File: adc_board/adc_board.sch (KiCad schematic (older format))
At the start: 47 parts, among them U4 HY3131, U8 ITX0505SA, U9 74HC595

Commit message: More work on ADC board schematics
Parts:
- removed R? (x3): R, symbol Device:R
- added C14, C7: 27nF, symbol Device:C
- added C19, C2, C25, C26, C3, C4, C6: C, symbol Device:C
- added F?: Fuse, symbol Device:Fuse
- added R10, R14, R3: 2.5M, symbol Device:R
- added R11: 20k, symbol Device:R
- added R17, R45, R62: 100, symbol Device:R
- added R2, R8, R9: 270k, symbol Device:R
- added R26: 56k, symbol Device:R
- added R28, R31: 90k, symbol Device:R
- added R30, R32: 10k, symbol Device:R
- added R34, R51, R52: 1k, symbol Device:R
- added R36: 1M, symbol Device:R
- added R76: 0, symbol Device:R
- R18: renamed from R?; value R -> 2.5M
- R19: renamed from R?; value R -> 1M
- R20: renamed from R?; value R -> 100k
- R21: renamed from R?; value R -> 10k
- R22, R24: renamed from R?; value R -> 1k
- R23: renamed from R?; value R -> 10M
- R?: value R -> 1
- Y?: value Crystal -> 4 MHz
- gave numbers to parts that had none: 2
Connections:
- net labels added: CNT, GND, VSSA
- wire segments 0 -> 142
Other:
- moved on the sheet: C02, C03, C04, C06, C07, D?, F?, K?, R19, R20, R21, R22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

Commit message: Map out U2 on ADC board
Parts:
- removed R?: 1, symbol Device:R
- added C?: CP, symbol Device:CP
- added R13, R15: 10k, symbol Device:R
- added R6: 100, symbol Device:R
- added R60: 750, symbol Device:R
- added R7: 1, symbol Device:R_Shunt
- added U2: SGM3157, Package_TO_SOT_SMD:SOT-363_SC-70-6, symbol Analog_Switch:FSA3157P6X
- R41: renamed from R?; value R -> 430
- R42: renamed from R?; value R -> 820
- U8: value ITX0505SA -> F0505S-1W
- gave numbers to parts that had none: 2
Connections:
- net labels added: PB1, U19_CTRL, VDD
- wire segments 142 -> 191
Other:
- note added: "VDD = 3.6 V"
- moved on the sheet: K?, R41, R42, U8, U9, U?

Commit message: Map out ADC board digital connections & DGND
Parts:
- removed U? (x5): ILD74, symbol Isolator:ILD74
- added C38, C42, C8, C?: C, symbol Device:C
- added D1, D2, D3, D4, D5: D, symbol Device:D
- added L1, L3, L4: Ferrite, symbol Device:L_Core_Ferrite
- added Q1, Q2, Q5: NPN, symbol Device:Q_NPN_BCE
- added R1, R46: 10, symbol Device:R
- added R16, R43, R44: 1k, symbol Device:R
- added R40, R?: 2k, symbol Device:R
- added R55: 330, symbol Device:R
- added R64, R65, R66, R75, R?: 470, symbol Device:R
- added U12: EL357, Package_DIP:DIP-4_W7.62mm, symbol Isolator:SFH617A-1
- added U15, U16: ELD207, Package_DIP:DIP-8_W7.62mm, symbol Isolator:LTV-827
- C13: renamed from C?; value CP -> 220uF
- gave numbers to parts that had none: 5
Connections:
- net labels added: +5V, GNDA, GNDD, GNDPWR, MCU_MISO, MCU_MOSI, MCU_NSS1, MCU_NSS2, MCU_SCK, MISO, MOSI, NSS1, NSS2, RL1_CTRL, RL2_CTRL, SCK, U1_CTRL, U2_CTRL, VDD_MCU
- wire segments 191 -> 316
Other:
- note added: "NOTE: GNDA = GNDD + 3.3V"
- note added: "Regulator voltage 3.6 V\nDiode drop 0.3 V"
- note added: "U3 is apparently overcurrent\nprotection for the low current side."
- note removed: "VDD = 3.6 V"
- moved on the sheet: C03, C05, C13, J?, R41, R42, U8, U?

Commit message: Map remaining connections on ADC board
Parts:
- removed D5: D, symbol Device:D
- removed F?: Polyfuse, symbol Device:Polyfuse
- added C10, C20, C21, C22, C30, C34, C41, C9: C, symbol Device:C
- added D5: Diode, symbol Device:D_x2_Serial_ACK
- added Q3, Q4: NPN, symbol Device:Q_NPN_BCE
- added R25: 100, symbol Device:R
- added R29, R35, R56: 2k, symbol Device:R
- added R5: PTC 1kohm, symbol Device:Thermistor_PTC
- added U17: MAX6071AAUT12, Package_TO_SOT_SMD:SOT-23-6, symbol Reference_Voltage:REF3230AMDBVREP
- U13: renamed from J?; value Conn_01x16 -> To MCU board
- gave numbers to parts that had none: 13
- renumbered C38 to C36
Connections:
- net +5V: now also R25.2
- net GNDA: now also C20.1, C21.2, D5.2 (common), Q4.3 (E)
- net GNDD: now also U9.13 (~OE), C20.2, C21.1, C22.2, C34.2, D5.1 (A), R29.2, R35.2, R56.2
- net MOSI: now also R29.1
- net NSS1: now also R56.1
- net SCK: now also R35.1
- net VDD: now also D5.3 (K)
- net at C14.1, R17.2: now also Q3.3 (E), R5.1
- net at R19.2, U4.39 (PA7): now also C41.1
- net at U4.4 (REFO): now also C9.2
- net at C3.2, R19.1, R20.1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: now also C41.2
- net VREF_1.25: now reaches U4.7 (PB6)
- net VREF_1.25: now also C10.2, U17.5 (OUT_S), U17.6 (OUT_F)
- net at RL1.8: now also R5.2
- net at Q1.2 (C): now also R46.2
- new net: C10.1, C30.2, C9.1, U17.1 (GNDF), U17.2 (GNDS)
- new net: C22.1, C30.1, C34.1, R25.1, U17.3 (ENABLE), U17.4 (VIN)
- new net: Q3.1 (B), Q3.2 (C), Q4.1 (B), Q4.2 (C)
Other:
- note added: "1.25 V reference"
- note added: "NOTE: GNDA is floating relative to GNDD,\nand usually settles at GNDA = VDD + 0.4V"
- note added: "VDD = 3.4 V"
- note removed: "NOTE: GNDA = GNDD + 3.3V"
- note removed: "Regulator voltage 3.6 V\nDiode drop 0.3 V"

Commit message: Clean up ADC board schematic
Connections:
- net GND is gone; now on net GNDA: C03.1 (Pin_1)
- net GNDA: now also R32.1; no longer R32.2
- net VDD: now also D2.1 (K), RL2.10
- net VSSA: now also C10.1, C30.2, C6.2, C8.1, C9.1, R55.2, U17.1 (GNDF), U17.2 (GNDS), U4.3 (AGND); no longer C6.1
- net PB2: now reaches C26.1, R52.1, U4.11 (PB2)
- net at U4.13 (ACM): now also C6.1; no longer C6.2
- net PB0: now reaches R11.2, U4.16 (PB0)
- net at U4.17 (PB8): now also R26.2
- net OP1N: now reaches U4.18 (OP1N)
- net OP1N: now also R28.2, R30.2; no longer R26.2
- net OP1O: now reaches C4.2, R28.1, U4.19 (OP1O)
- net OP2N: now reaches R31.2
- net OP2N: now also R32.2, U4.20 (OP2N); no longer U4.21 (OP2O)
- net PB5: now reaches C26.2, R51.1, U4.8 (PB5)
- net PB4: now reaches C4.1, R36.2, U4.9 (PB4)
- net at RL1.4: now also RL1.7
- net at Q2.2 (C): now also R1.2
- new net OP2O: R31.1, U4.21 (OP2O)
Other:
- note added: "4-wire resistance sense"
- note added: "Current measurement"
- note added: "Power supply isolation"
- note added: "Relay control"
- note added: "SPI isolation"
- note added: "U3 is overcurrent protection\nfor the low current shunts."
- note added: "Voltage measurement"
- note removed: "U3 is apparently overcurrent\nprotection for the low current side."
- moved on the sheet: C02, C03, C04, C05, C06, C07, C10, C13, C14, C19, C2, C20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

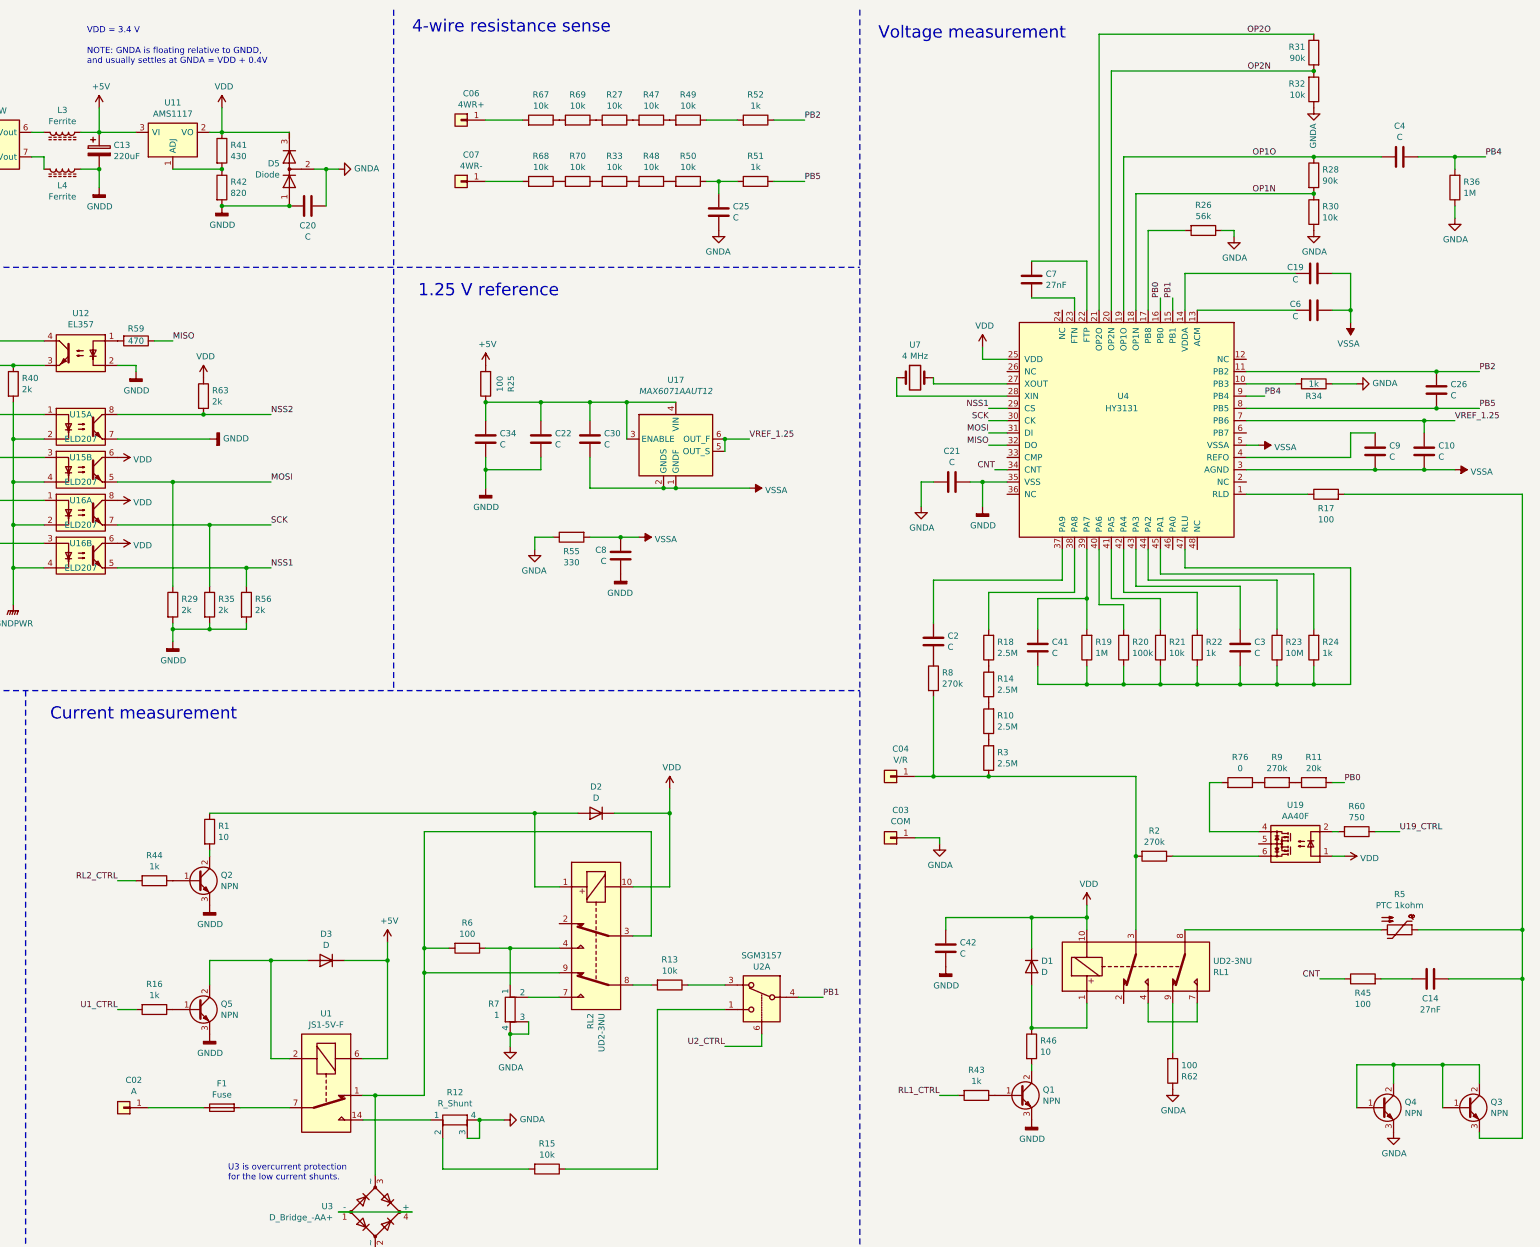
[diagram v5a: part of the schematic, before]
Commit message: ADC board schematic: fix GNDA/VSSA mixup
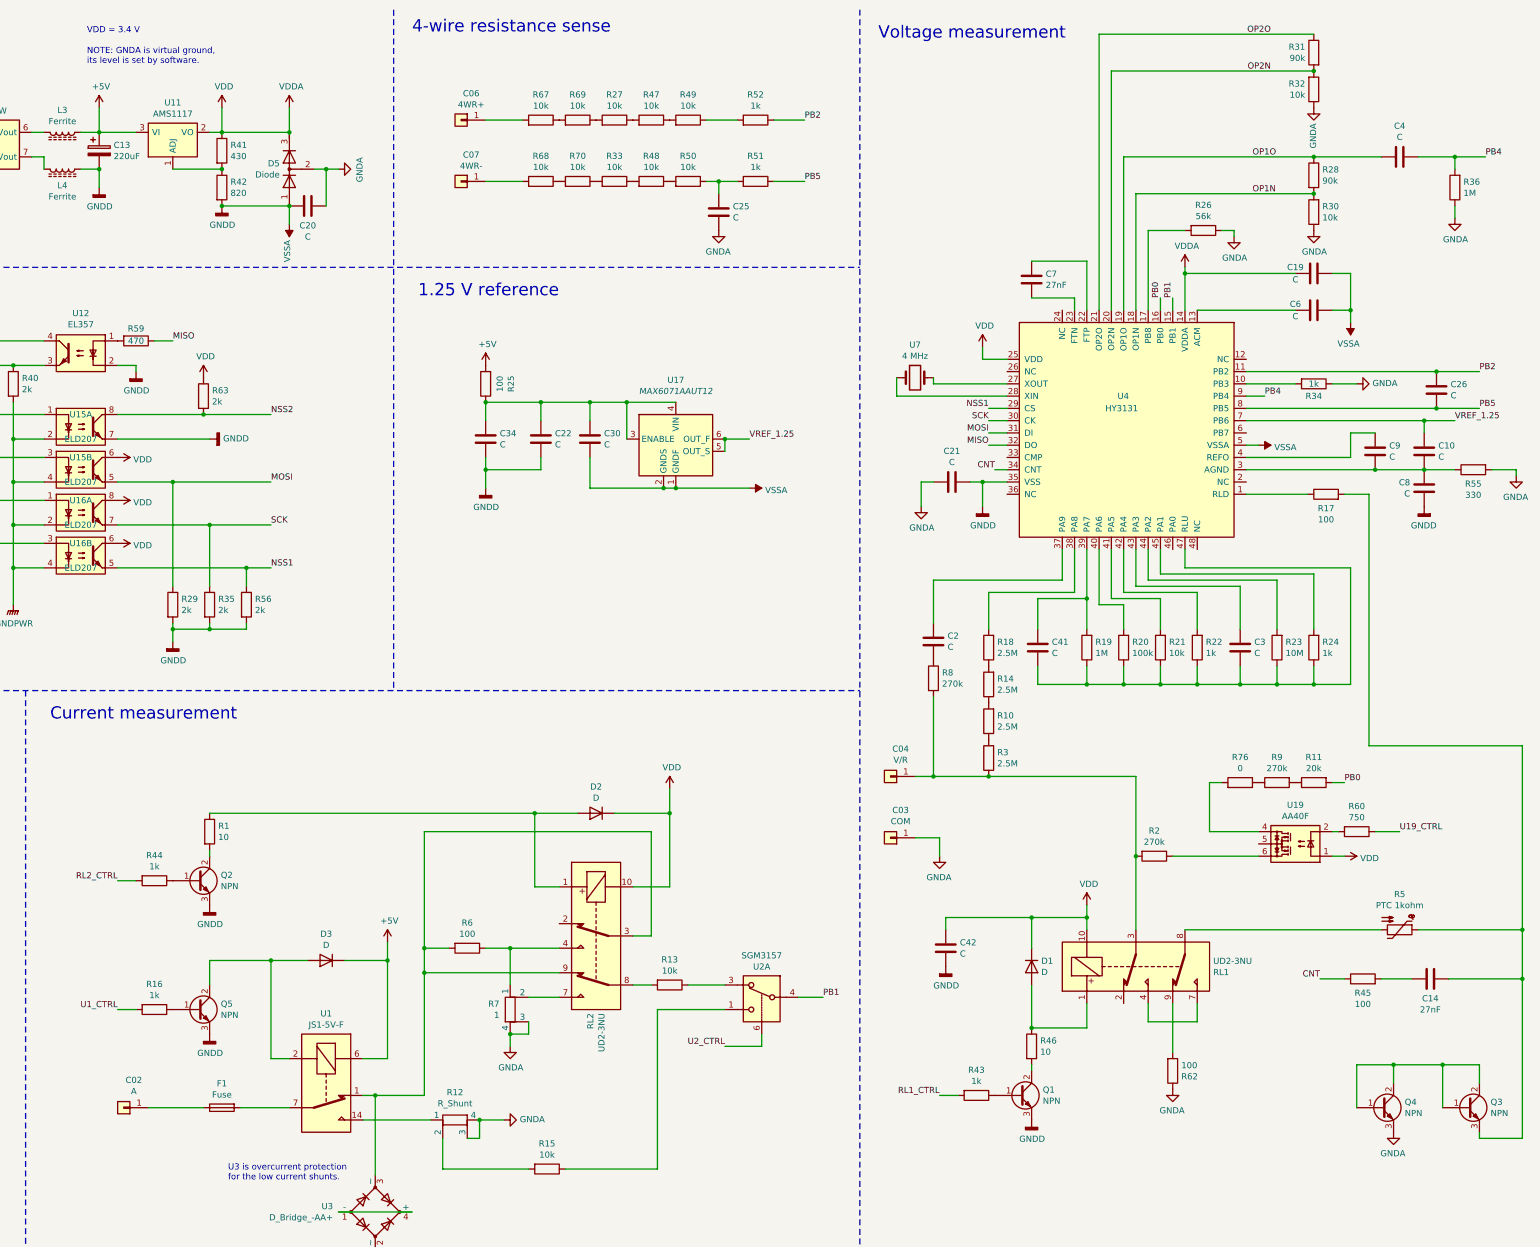
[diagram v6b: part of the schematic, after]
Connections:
- net GNDA: now also R55.2; no longer R55.1
- net GNDD: now also C19.1, C30.2, C6.2, U17.1 (GNDF), U17.2 (GNDS), U4.5 (VSSA)
- net VDD: now also C19.2, U4.14 (VDDA)
- removed net VSSA: C10.1, C19.1, C30.2, C6.2, C8.1, C9.1, R55.2, U17.1 (GNDF), U17.2 (GNDS), U4.3 (AGND), U4.5 (VSSA)
- new net: C10.1, C8.1, C9.1, R55.1, U4.3 (AGND)
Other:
- note added: "NOTE: GNDA is virtual ground,\nits level is set by software."
- note removed: "NOTE: GNDA is floating relative to GNDD,\nand usually settles at GNDA = VDD + 0.4V"
- moved on the sheet: C8, R55
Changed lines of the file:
@@
 Sheet 1 1
 Title "XDM2041 ADC board"
-Date "2021-08-12"
+Date "2022-01-18"
 Rev ""
 Comp ""
@@
 	11900 6000 12200 6000
 Wire Wire Line
-	10400 7300 10400 7250
-Wire Wire Line
 	10400 7250 10200 7250
 $Comp
@@
 Connection ~ 3550 1500
 Text Notes 3450 950  0    50   ~ 0
-NOTE: GNDA is floating relative to GNDD,\nand usually settles at GNDA = VDD + 0.4V
-$Comp
-L power:GNDA #PWR0108
-U 1 1 6140A326
-P 5500 1800
-F 0 "#PWR0108" H 5500 1550 50  0001 C CNN
-F 1 "GNDA" V 5505 1672 50  0000 R CNN
-F 2 "" H 5500 1800 50  0001 C CNN
-F 3 "" H 5500 1800 50  0001 C CNN
-	1    5500 1800
-	0    -1   -1   0
-$EndComp
+NOTE: GNDA is virtual ground,\nits level is set by software.
 $Comp
 L power:GNDA #PWR0109
@@
 $EndComp
 $Comp
-L power:GNDA #PWR0121
-U 1 1 61447E7F
-P 12300 9300
-F 0 "#PWR0121" H 12300 9050 50  0001 C CNN
-F 1 "GNDA" H 12305 9127 50  0000 C CNN
-F 2 "" H 12300 9300 50  0001 C CNN
-F 3 "" H 12300 9300 50  0001 C CNN
-	1    12300 9300
-	1    0    0    -1
-$EndComp
-$Comp
 L power:GNDA #PWR0122
 U 1 1 6144821F
@@
 $EndComp
 $Comp
-L power:GNDA #PWR0125
-U 1 1 61448B22
-P 14600 2200
-F 0 "#PWR0125" H 14600 1950 50  0001 C CNN
-F 1 "GNDA" H 14605 2027 50  0000 C CNN
-F 2 "" H 14600 2200 50  0001 C CNN
-F 3 "" H 14600 2200 50  0001 C CNN
-	1    14600 2200
-	1    0    0    -1
-$EndComp
-$Comp
 L power:GNDA #PWR0126
 U 1 1 61449089
@@
 Wire Wire Line
 	5500 1800 5400 1800
-Wire Wire Line
-	5100 2100 4550 2100
 Connection ~ 4550 2100
 Wire Wire Line
@@
 F 3 "~" H 14000 9450 50  0001 C CNN
 	1    14000 9450
-	1    0    0    -1
-$EndComp
-$Comp
-L power:GNDA #PWR0145
-U 1 1 61FC7B1B
-P 14100 9650
-F 0 "#PWR0145" H 14100 9400 50  0001 C CNN
-F 1 "GNDA" H 14105 9477 50  0000 C CNN
-F 2 "" H 14100 9650 50  0001 C CNN
-F 3 "" H 14100 9650 50  0001 C CNN
-	1    14100 9650
 	1    0    0    -1
 $EndComp
@@
 $EndComp
 Wire Wire Line
-	15150 4450 15150 8000
-Wire Wire Line
-	13700 4450 15150 4450
+	13700 4450 13900 4450
 Connection ~ 15150 8000
 Wire Wire Line
@@
 Wire Wire Line
 	13750 2950 13750 3050
-$Comp
-L power:VSSA #PWR?
-U 1 1 623F77D1
-P 14600 4250
-F 0 "#PWR?" H 14600 4100 50  0001 C CNN
-F 1 "VSSA" V 14617 4378 50  0000 L CNN
-F 2 "" H 14600 4250 50  0001 C CNN
-F 3 "" H 14600 4250 50  0001 C CNN
-	1    14600 4250
-	0    1    1    0
-$EndComp
 Wire Wire Line
 	14600 4250 14350 4250
@@
 Wire Wire Line
 	11700 700  13450 700
-$Comp
-L power:GNDA #PWR?
-U 1 1 628521CC
-P 10400 7300
-F 0 "#PWR?" H 10400 7050 50  0001 C CNN
-F 1 "GNDA" H 10405 7127 50  0000 C CNN
-F 2 "" H 10400 7300 50  0001 C CNN
-F 3 "" H 10400 7300 50  0001 C CNN
-	1    10400 7300
-	1    0    0    -1
-$EndComp
 $Comp
 L power:VSSA #PWR?
@@
 F 3 "" H 8850 4400 50  0001 C CNN
 	1    8850 4400
-	0    1    1    0
-$EndComp
-Connection ~ 7800 4800
-Wire Wire Line
-	7950 4800 7800 4800
-$Comp
-L power:VSSA #PWR?
-U 1 1 6246EB29
-P 7950 4800
-F 0 "#PWR?" H 7950 4650 50  0001 C CNN
-F 1 "VSSA" V 7967 4928 50  0000 L CNN
-F 2 "" H 7950 4800 50  0001 C CNN
-F 3 "" H 7950 4800 50  0001 C CNN
-	1    7950 4800
 	0    1    1    0
 $EndComp
@@
 L power:GNDD #PWR0107
 U 1 1 61409269
-P 7800 5100
-F 0 "#PWR0107" H 7800 4850 50  0001 C CNN
-F 1 "GNDD" H 7804 4945 50  0000 C CNN
-F 2 "" H 7800 5100 50  0001 C CNN
-F 3 "" H 7800 5100 50  0001 C CNN
-	1    7800 5100
+P 14350 4550
+F 0 "#PWR0107" H 14350 4300 50  0001 C CNN
+F 1 "GNDD" H 14354 4395 50  0000 C CNN
+F 2 "" H 14350 4550 50  0001 C CNN
+F 3 "" H 14350 4550 50  0001 C CNN
+	1    14350 4550
 	-1   0    0    -1
 $EndComp
-Wire Wire Line
-	7100 4800 7250 4800
-Wire Wire Line
-	7100 4900 7100 4800
-$Comp
-L power:GNDA #PWR0106
-U 1 1 613FA924
-P 7100 4900
-F 0 "#PWR0106" H 7100 4650 50  0001 C CNN
-F 1 "GNDA" H 7105 4727 50  0000 C CNN
-F 2 "" H 7100 4900 50  0001 C CNN
-F 3 "" H 7100 4900 50  0001 C CNN
-	1    7100 4900
-	-1   0    0    -1
-$EndComp
-Wire Wire Line
-	7550 4800 7800 4800
 $Comp
 L Device:R R55
 U 1 1 613DD030
-P 7400 4800
-F 0 "R55" V 7515 4800 50  0000 C CNN
-F 1 "330" V 7606 4800 50  0000 C CNN
-F 2 "" V 7330 4800 50  0001 C CNN
-F 3 "~" H 7400 4800 50  0001 C CNN
-	1    7400 4800
+P 14750 4250
+F 0 "R55" V 14865 4250 50  0000 C CNN
+F 1 "330" V 14956 4250 50  0000 C CNN
+F 2 "" V 14680 4250 50  0001 C CNN
+F 3 "~" H 14750 4250 50  0001 C CNN
+	1    14750 4250
 	0    -1   1    0
 $EndComp
@@
 L Device:C C8
 U 1 1 613DB47A
-P 7800 4950
-F 0 "C8" H 7915 4996 50  0000 L CNN
-F 1 "C" H 7915 4905 50  0000 L CNN
-F 2 "" H 7838 4800 50  0001 C CNN
-F 3 "~" H 7800 4950 50  0001 C CNN
-	1    7800 4950
+P 14350 4400
+F 0 "C8" H 14465 4446 50  0000 L CNN
+F 1 "C" H 14465 4355 50  0000 L CNN
+F 2 "" H 14388 4250 50  0001 C CNN
+F 3 "~" H 14350 4400 50  0001 C CNN
+	1    14350 4400
 	-1   0    0    -1
 $EndComp
@@
 Text Notes 9900 750  0    100  ~ 0
 Voltage measurement
+$Comp
+L power:VSSA #PWR?
+U 1 1 61E9AF63
+P 5100 2250
+F 0 "#PWR?" H 5100 2100 50  0001 C CNN
+F 1 "VSSA" V 5117 2378 50  0000 L CNN
+F 2 "" H 5100 2250 50  0001 C CNN
+F 3 "" H 5100 2250 50  0001 C CNN
+	1    5100 2250
+	-1   0    0    1
+$EndComp
+$Comp
+L power:VDDA #PWR?
+U 1 1 61E9CF51
+P 12400 2600
+F 0 "#PWR?" H 12400 2450 50  0001 C CNN
+F 1 "VDDA" H 12415 2773 50  0000 C CNN
+F 2 "" H 12400 2600 50  0001 C CNN
+F 3 "" H 12400 2600 50  0001 C CNN
+	1    12400 2600
+	1    0    0    -1
+$EndComp
+Wire Wire Line
+	12400 2600 12400 2650
+Connection ~ 12400 2650
+$Comp
+L power:VDDA #PWR?
+U 1 1 61EC0AAB
+P 5100 1300
+F 0 "#PWR?" H 5100 1150 50  0001 C CNN
+F 1 "VDDA" H 5115 1473 50  0000 C CNN
+F 2 "" H 5100 1300 50  0001 C CNN
+F 3 "" H 5100 1300 50  0001 C CNN
+	1    5100 1300
+	1    0    0    -1
+$EndComp
+Wire Wire Line
+	5100 1300 5100 1500
+Connection ~ 5100 1500
+Wire Wire Line
+	5100 2250 5100 2100
+Wire Wire Line
+	4550 2100 5100 2100
+Wire Wire Line
+	10400 7250 10400 7400
+$Comp
+L power:GNDA #PWR?
+U 1 1 61F2EC55
+P 15100 4300
+F 0 "#PWR?" H 15100 4050 50  0001 C CNN
+F 1 "GNDA" H 15105 4127 50  0000 C CNN
+F 2 "" H 15100 4300 50  0001 C CNN
+F 3 "" H 15100 4300 50  0001 C CNN
+	1    15100 4300
+	-1   0    0    -1
+$EndComp
+$Comp
+L power:GNDA #PWR?
+U 1 1 61F9C4AA
+P 10400 7400
+F 0 "#PWR?" H 10400 7150 50  0001 C CNN
+F 1 "GNDA" H 10405 7227 50  0000 C CNN
+F 2 "" H 10400 7400 50  0001 C CNN
+F 3 "" H 10400 7400 50  0001 C CNN
+	1    10400 7400
+	-1   0    0    -1
+$EndComp
+$Comp
+L power:GNDA #PWR?
+U 1 1 61F9CA08
+P 12300 9300
+F 0 "#PWR?" H 12300 9050 50  0001 C CNN
+F 1 "GNDA" H 12305 9127 50  0000 C CNN
+F 2 "" H 12300 9300 50  0001 C CNN
+F 3 "" H 12300 9300 50  0001 C CNN
+	1    12300 9300
+	-1   0    0    -1
+$EndComp
+$Comp
+L power:GNDA #PWR?
+U 1 1 61F9CDA0
+P 14100 9650
+F 0 "#PWR?" H 14100 9400 50  0001 C CNN
+F 1 "GNDA" H 14105 9477 50  0000 C CNN
+F 2 "" H 14100 9650 50  0001 C CNN
+F 3 "" H 14100 9650 50  0001 C CNN
+	1    14100 9650
+	-1   0    0    -1
+$EndComp
+$Comp
+L power:GNDA #PWR?
+U 1 1 61F9D03E
+P 5500 1800
+F 0 "#PWR?" H 5500 1550 50  0001 C CNN
+F 1 "GNDA" H 5505 1627 50  0000 C CNN
+F 2 "" H 5500 1800 50  0001 C CNN
+F 3 "" H 5500 1800 50  0001 C CNN
+	1    5500 1800
+	0    -1   1    0
+$EndComp
+$Comp
+L power:GNDA #PWR?
+U 1 1 61F9D57E
+P 14600 2200
+F 0 "#PWR?" H 14600 1950 50  0001 C CNN
+F 1 "GNDA" H 14605 2027 50  0000 C CNN
+F 2 "" H 14600 2200 50  0001 C CNN
+F 3 "" H 14600 2200 50  0001 C CNN
+	1    14600 2200
+	1    0    0    -1
+$EndComp
+Wire Wire Line
+	15150 6500 13900 6500
+Wire Wire Line
+	13900 6500 13900 4450
+Wire Wire Line
+	15150 6500 15150 8000
+Wire Wire Line
+	15100 4300 15100 4250
+Wire Wire Line
+	15100 4250 14900 4250
 $EndSCHEMATC
